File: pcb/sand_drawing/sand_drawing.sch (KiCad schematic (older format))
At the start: 19 parts, among them J0 12V GND, J1 Stepper1, J2 Stepper2, J3 Opto 1, J4 Opto 2, J5 ESP POWER, J6 Unused Pins, U1 WeMos_D1_mini, U2 LD1117

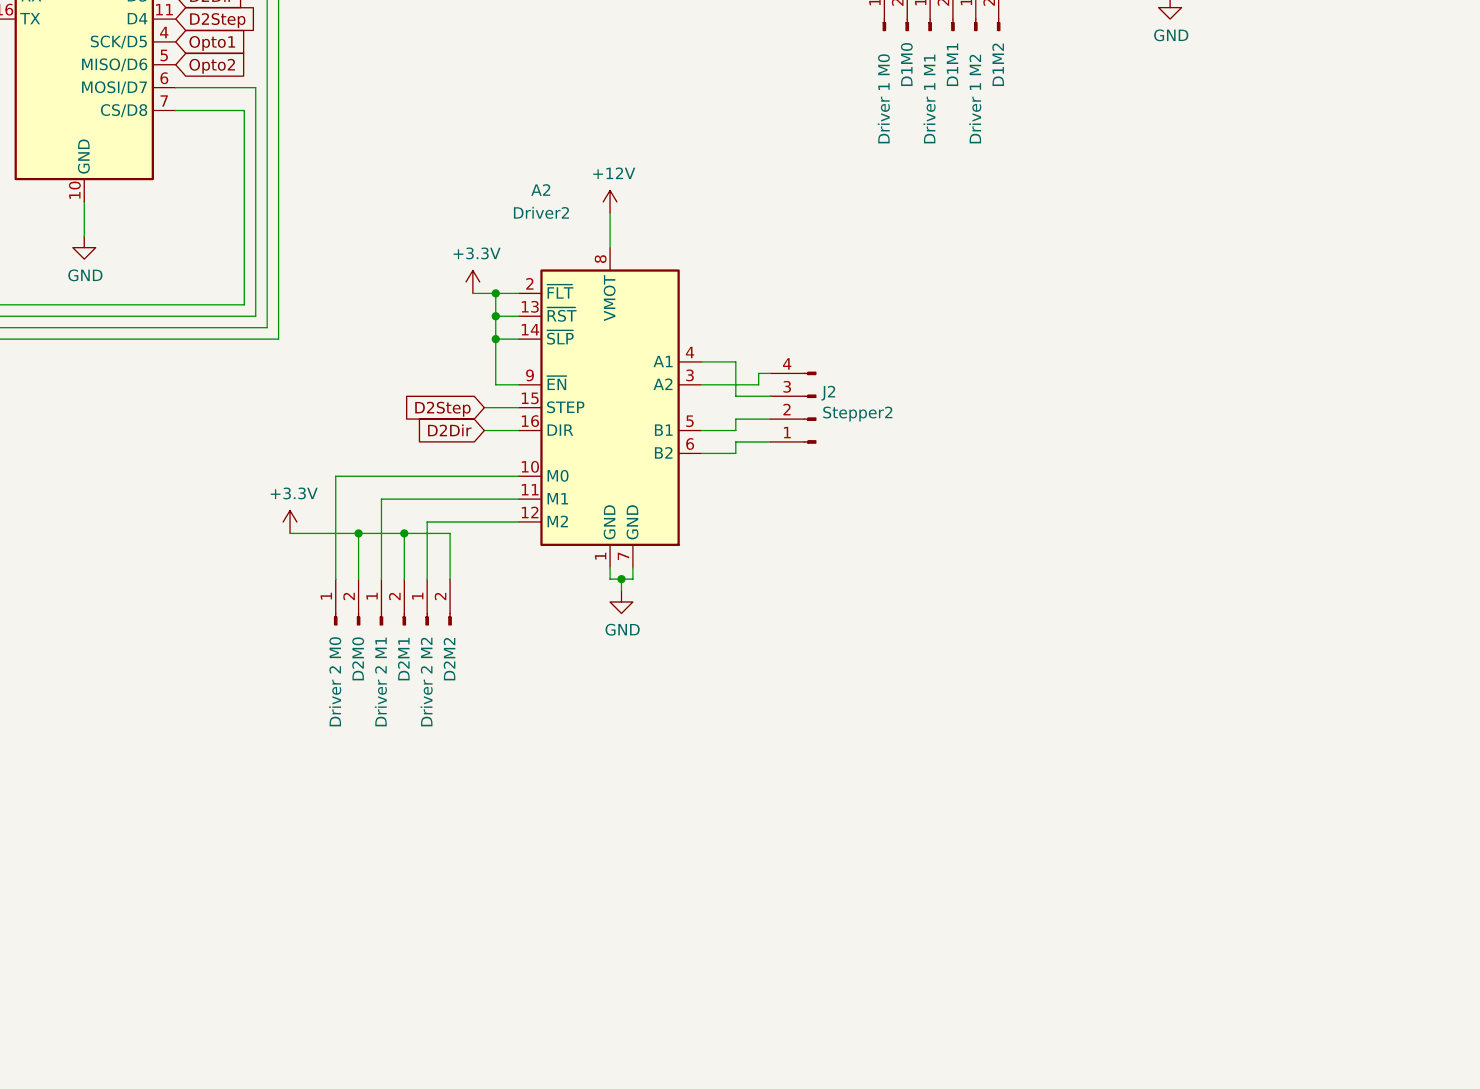
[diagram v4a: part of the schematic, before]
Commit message: More work on adding the esp32 .
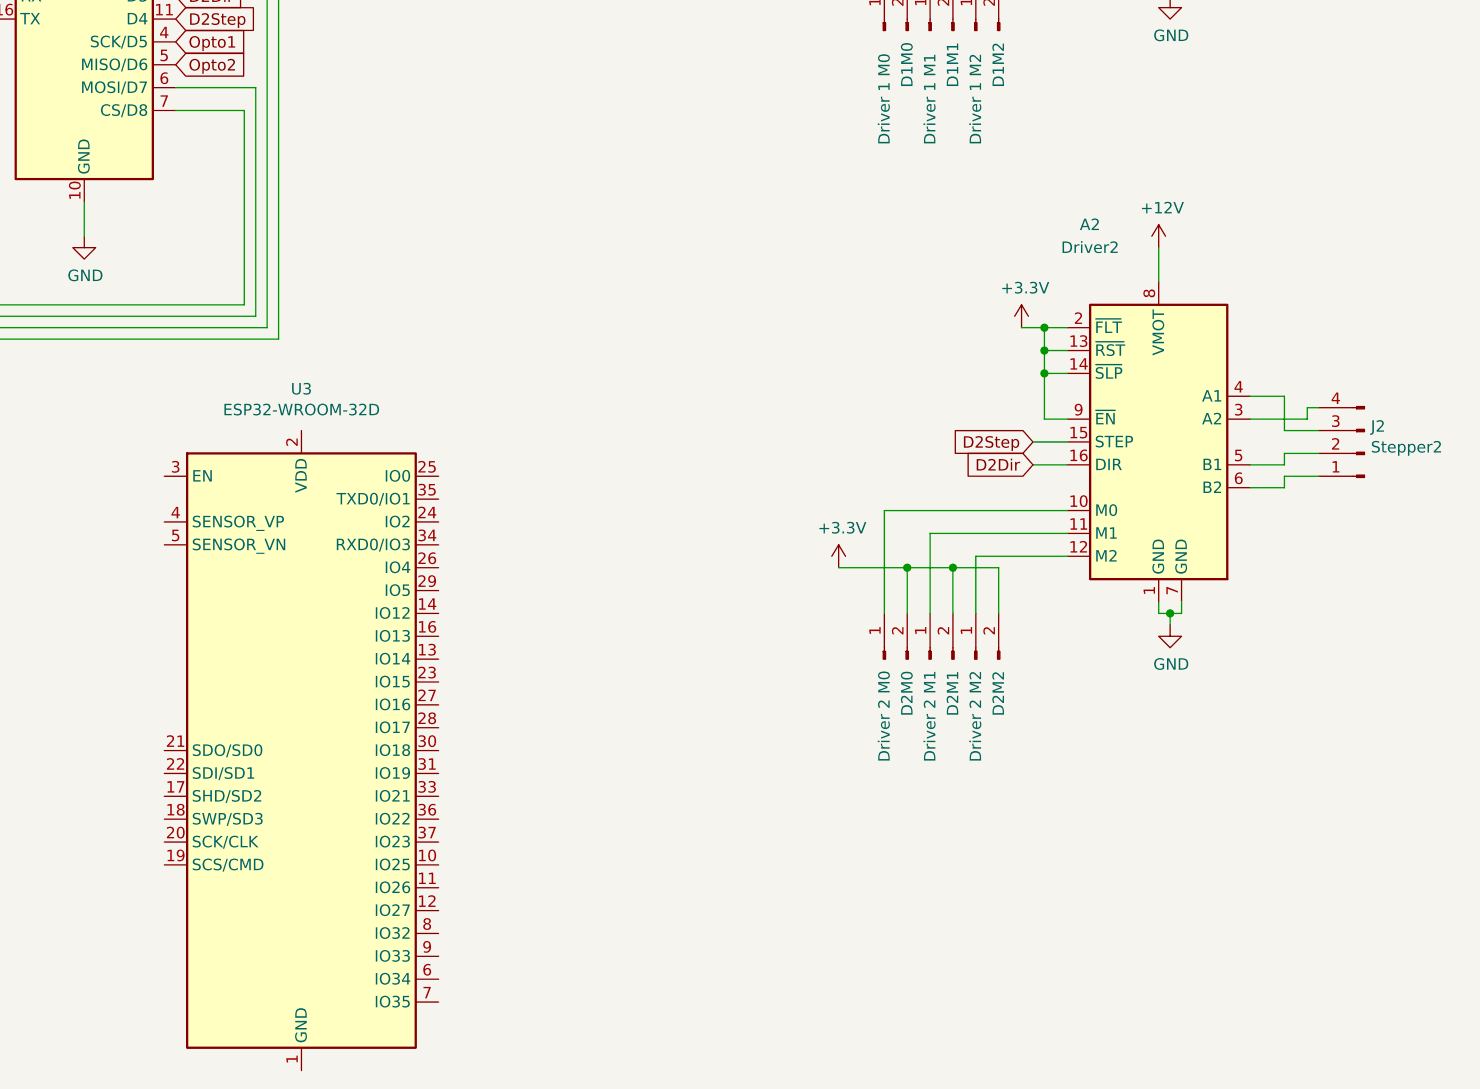
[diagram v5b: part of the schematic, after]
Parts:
- added U3: ESP32-WROOM-32D, Custom:ESP32-WROOM-32, symbol RF_Module:ESP32-WROOM-32D
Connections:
- new net: U3.1 (GND), U3.15 (GND), U3.38 (GND), U3.39 (GND)
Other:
- moved on the sheet: A2, D2M0, D2M1, D2M2, J2
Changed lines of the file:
@@
 L Driver_Motor:Pololu_Breakout_DRV8825 A2
 U 1 1 5E987B88
-P 5600 4200
-F 0 "A2" H 5300 5050 50  0000 C CNN
-F 1 "Driver2" H 5300 4950 50  0000 C CNN
-F 2 "Modules:Pololu_Breakout-16_15.2x20.3mm" H 5800 3400 50  0001 L CNN
-F 3 "https://www.pololu.com/product/2982" H 5700 3900 50  0001 C CNN
-	1    5600 4200
+P 8000 4350
+F 0 "A2" H 7700 5200 50  0000 C CNN
+F 1 "Driver2" H 7700 5100 50  0000 C CNN
+F 2 "Modules:Pololu_Breakout-16_15.2x20.3mm" H 8200 3550 50  0001 L CNN
+F 3 "https://www.pololu.com/product/2982" H 8100 4050 50  0001 C CNN
+	1    8000 4350
 	1    0    0    -1
 $EndComp
@@
 L Connector:Conn_01x04_Male J2
 U 1 1 5E98E54C
-P 6500 4350
-F 0 "J2" H 6472 4232 50  0000 R CNN
-F 1 "Stepper2" H 6472 4323 50  0000 R CNN
-F 2 "Socket_Strips:Socket_Strip_Straight_1x04_Pitch2.54mm" H 6500 4350 50  0001 C CNN
-F 3 "~" H 6500 4350 50  0001 C CNN
-	1    6500 4350
+P 8900 4500
+F 0 "J2" H 8872 4382 50  0000 R CNN
+F 1 "Stepper2" H 8872 4473 50  0000 R CNN
+F 2 "Socket_Strips:Socket_Strip_Straight_1x04_Pitch2.54mm" H 8900 4500 50  0001 C CNN
+F 3 "~" H 8900 4500 50  0001 C CNN
+	1    8900 4500
 	-1   0    0    1
 $EndComp
@@
 	8550 1850 8700 1850
 Wire Wire Line
-	6000 4100 6150 4100
-Wire Wire Line
-	6000 4400 6150 4400
-Wire Wire Line
-	6150 4400 6150 4350
-Wire Wire Line
-	6150 4350 6300 4350
-Wire Wire Line
-	6000 4500 6150 4500
-Wire Wire Line
-	6150 4500 6150 4450
-Wire Wire Line
-	6150 4450 6300 4450
+	8400 4250 8550 4250
+Wire Wire Line
+	8400 4550 8550 4550
+Wire Wire Line
+	8550 4550 8550 4500
+Wire Wire Line
+	8550 4500 8700 4500
+Wire Wire Line
+	8400 4650 8550 4650
+Wire Wire Line
+	8550 4650 8550 4600
+Wire Wire Line
+	8550 4600 8700 4600
 Wire Wire Line
 	7500 1200 7400 1200
 Wire Wire Line
-	5200 4200 5100 4200
-Wire Wire Line
-	5200 4000 5100 4000
-Wire Wire Line
-	5100 4000 5100 4200
-Wire Wire Line
-	5200 3900 5100 3900
-Wire Wire Line
-	5100 3900 5100 4000
-Connection ~ 5100 4000
-Wire Wire Line
-	5100 3800 5100 3900
-Connection ~ 5100 3900
+	7600 4350 7500 4350
+Wire Wire Line
+	7600 4150 7500 4150
+Wire Wire Line
+	7500 4150 7500 4350
+Wire Wire Line
+	7600 4050 7500 4050
+Wire Wire Line
+	7500 4050 7500 4150
+Connection ~ 7500 4150
+Wire Wire Line
+	7500 3950 7500 4050
+Connection ~ 7500 4050
 Wire Wire Line
 	7600 1600 7500 1600
@@
 L power:GND #PWR0101
 U 1 1 5E9A89B2
-P 5650 5100
-F 0 "#PWR0101" H 5650 4850 50  0001 C CNN
-F 1 "GND" H 5655 4927 50  0000 C CNN
-F 2 "" H 5650 5100 50  0001 C CNN
-F 3 "" H 5650 5100 50  0001 C CNN
-	1    5650 5100
+P 8050 5250
+F 0 "#PWR0101" H 8050 5000 50  0001 C CNN
+F 1 "GND" H 8055 5077 50  0000 C CNN
+F 2 "" H 8050 5250 50  0001 C CNN
+F 3 "" H 8050 5250 50  0001 C CNN
+	1    8050 5250
 	1    0    0    -1
 $EndComp
@@
 Connection ~ 8050 2450
 Wire Wire Line
-	5600 5000 5600 5050
-Wire Wire Line
-	5600 5050 5650 5050
-Wire Wire Line
-	5650 5050 5650 5100
-Wire Wire Line
-	5650 5050 5700 5050
-Wire Wire Line
-	5700 5050 5700 5000
-Connection ~ 5650 5050
+	8000 5150 8000 5200
+Wire Wire Line
+	8000 5200 8050 5200
+Wire Wire Line
+	8050 5200 8050 5250
+Wire Wire Line
+	8050 5200 8100 5200
+Wire Wire Line
+	8100 5200 8100 5150
+Connection ~ 8050 5200
 $Comp
 L power:+12V #PWR0103
 U 1 1 5E9C6646
-P 5600 3450
-F 0 "#PWR0103" H 5600 3300 50  0001 C CNN
-F 1 "+12V" H 5615 3623 50  0000 C CNN
-F 2 "" H 5600 3450 50  0001 C CNN
-F 3 "" H 5600 3450 50  0001 C CNN
-	1    5600 3450
+P 8000 3600
+F 0 "#PWR0103" H 8000 3450 50  0001 C CNN
+F 1 "+12V" H 8015 3773 50  0000 C CNN
+F 2 "" H 8000 3600 50  0001 C CNN
+F 3 "" H 8000 3600 50  0001 C CNN
+	1    8000 3600
 	1    0    0    -1
 $EndComp
@@
 Connection ~ 7500 1200
 Wire Wire Line
-	5200 3800 5100 3800
-Wire Wire Line
-	5000 3800 5100 3800
-Connection ~ 5100 3800
+	7600 3950 7500 3950
+Wire Wire Line
+	7400 3950 7500 3950
+Connection ~ 7500 3950
 $Comp
 L Connector:Conn_01x03_Male J3
@@
 L power:+3.3V #PWR0108
 U 1 1 5E9FDAD5
-P 5000 3800
-F 0 "#PWR0108" H 5000 3650 50  0001 C CNN
-F 1 "+3.3V" H 5015 3973 50  0000 C CNN
-F 2 "" H 5000 3800 50  0001 C CNN
-F 3 "" H 5000 3800 50  0001 C CNN
-	1    5000 3800
+P 7400 3950
+F 0 "#PWR0108" H 7400 3800 50  0001 C CNN
+F 1 "+3.3V" H 7415 4123 50  0000 C CNN
+F 2 "" H 7400 3950 50  0001 C CNN
+F 3 "" H 7400 3950 50  0001 C CNN
+	1    7400 3950
 	1    0    0    -1
 $EndComp
@@
 	8600 1550 8700 1550
 Wire Wire Line
-	6150 4250 6300 4250
-Wire Wire Line
-	6150 4100 6150 4250
-Wire Wire Line
-	6300 4150 6250 4150
-Wire Wire Line
-	6250 4150 6250 4200
-Wire Wire Line
-	6250 4200 6000 4200
+	8550 4400 8700 4400
+Wire Wire Line
+	8550 4250 8550 4400
+Wire Wire Line
+	8700 4300 8650 4300
+Wire Wire Line
+	8650 4300 8650 4350
+Wire Wire Line
+	8650 4350 8400 4350
 $Comp
 L Connector_Generic:Conn_02x04_Top_Bottom J6
@@
 L Connector:Conn_01x02_Male D2M1
 U 1 1 5E9C5CF2
-P 4600 5250
-F 0 "D2M1" H 4450 5150 50  0000 C CNN
-F 1 "Driver 2 M1" H 4350 5250 50  0000 C CNN
-F 2 "Socket_Strips:Socket_Strip_Straight_1x02_Pitch2.54mm" H 4600 5250 50  0001 C CNN
-F 3 "~" H 4600 5250 50  0001 C CNN
-	1    4600 5250
+P 7000 5400
+F 0 "D2M1" H 6850 5300 50  0000 C CNN
+F 1 "Driver 2 M1" H 6750 5400 50  0000 C CNN
+F 2 "Socket_Strips:Socket_Strip_Straight_1x02_Pitch2.54mm" H 7000 5400 50  0001 C CNN
+F 3 "~" H 7000 5400 50  0001 C CNN
+	1    7000 5400
 	0    -1   -1   0
 $EndComp
@@
 L Connector:Conn_01x02_Male D2M2
 U 1 1 5E9C5F13
-P 4800 5250
-F 0 "D2M2" H 4650 5150 50  0000 C CNN
-F 1 "Driver 2 M2" H 4550 5250 50  0000 C CNN
-F 2 "Socket_Strips:Socket_Strip_Straight_1x02_Pitch2.54mm" H 4800 5250 50  0001 C CNN
-F 3 "~" H 4800 5250 50  0001 C CNN
-	1    4800 5250
+P 7200 5400
+F 0 "D2M2" H 7050 5300 50  0000 C CNN
+F 1 "Driver 2 M2" H 6950 5400 50  0000 C CNN
+F 2 "Socket_Strips:Socket_Strip_Straight_1x02_Pitch2.54mm" H 7200 5400 50  0001 C CNN
+F 3 "~" H 7200 5400 50  0001 C CNN
+	1    7200 5400
 	0    -1   -1   0
 $EndComp
@@
 	1400 5550 1400 4800
 Wire Wire Line
-	5200 4600 4400 4600
-Wire Wire Line
-	4400 4600 4400 5050
-Wire Wire Line
-	4600 5050 4600 4700
-Wire Wire Line
-	4600 4700 5200 4700
-Wire Wire Line
-	5200 4800 4800 4800
-Wire Wire Line
-	4800 4800 4800 5050
+	7600 4750 6800 4750
+Wire Wire Line
+	6800 4750 6800 5200
+Wire Wire Line
+	7000 5200 7000 4850
+Wire Wire Line
+	7000 4850 7600 4850
+Wire Wire Line
+	7600 4950 7200 4950
+Wire Wire Line
+	7200 4950 7200 5200
 $Comp
 L power:+3.3V #PWR0116
 U 1 1 5EA0D498
-P 4200 4850
-F 0 "#PWR0116" H 4200 4700 50  0001 C CNN
-F 1 "+3.3V" H 4215 5023 50  0000 C CNN
-F 2 "" H 4200 4850 50  0001 C CNN
-F 3 "" H 4200 4850 50  0001 C CNN
-	1    4200 4850
-	1    0    0    -1
-$EndComp
-Wire Wire Line
-	4500 4850 4500 5050
-Wire Wire Line
-	4900 4850 4900 5050
-Wire Wire Line
-	4500 4850 4700 4850
-Connection ~ 4500 4850
-Wire Wire Line
-	4700 5050 4700 4850
-Connection ~ 4700 4850
-Wire Wire Line
-	4700 4850 4900 4850
-Wire Wire Line
-	4200 4850 4500 4850
+P 6600 5000
+F 0 "#PWR0116" H 6600 4850 50  0001 C CNN
+F 1 "+3.3V" H 6615 5173 50  0000 C CNN
+F 2 "" H 6600 5000 50  0001 C CNN
+F 3 "" H 6600 5000 50  0001 C CNN
+	1    6600 5000
+	1    0    0    -1
+$EndComp
+Wire Wire Line
+	6900 5000 6900 5200
+Wire Wire Line
+	7300 5000 7300 5200
+Wire Wire Line
+	6900 5000 7100 5000
+Connection ~ 6900 5000
+Wire Wire Line
+	7100 5200 7100 5000
+Connection ~ 7100 5000
+Wire Wire Line
+	7100 5000 7300 5000
+Wire Wire Line
+	6600 5000 6900 5000
 Wire Wire Line
 	8000 850  8000 1000
 Wire Wire Line
-	5600 3600 5600 3450
+	8000 3750 8000 3600
 $Comp
 L Connector:Conn_01x02_Male D1M0
@@
 L Connector:Conn_01x02_Male D2M0
 U 1 1 5E99CB34
-P 4400 5250
-F 0 "D2M0" H 4250 5150 50  0000 C CNN
-F 1 "Driver 2 M0" H 4150 5250 50  0000 C CNN
-F 2 "Socket_Strips:Socket_Strip_Straight_1x02_Pitch2.54mm" H 4400 5250 50  0001 C CNN
-F 3 "~" H 4400 5250 50  0001 C CNN
-	1    4400 5250
+P 6800 5400
+F 0 "D2M0" H 6650 5300 50  0000 C CNN
+F 1 "Driver 2 M0" H 6550 5400 50  0000 C CNN
+F 2 "Socket_Strips:Socket_Strip_Straight_1x02_Pitch2.54mm" H 6800 5400 50  0001 C CNN
+F 3 "~" H 6800 5400 50  0001 C CNN
+	1    6800 5400
 	0    -1   -1   0
 $EndComp
@@
 Text GLabel 3700 2600 2    50   Input ~ 0
 D2Step
-Text GLabel 5050 4400 0    50   Input ~ 0
+Text GLabel 7450 4550 0    50   Input ~ 0
 D2Dir
-Text GLabel 5050 4300 0    50   Input ~ 0
+Text GLabel 7450 4450 0    50   Input ~ 0
 D2Step
 Wire Wire Line
-	5200 4300 5050 4300
-Wire Wire Line
-	5200 4400 5050 4400
+	7600 4450 7450 4450
+Wire Wire Line
+	7600 4550 7450 4550
 $Comp
 L Connector:Conn_01x02_Male D1M2
@@
 	0    -1   -1   0
 $EndComp
+$Comp
+L RF_Module:ESP32-WROOM-32D U3
+U 1 1 5EC68010
+P 4250 5800
+F 0 "U3" H 4250 7381 50  0000 C CNN
+F 1 "ESP32-WROOM-32D" H 4250 7290 50  0000 C CNN
+F 2 "Custom:ESP32-WROOM-32" H 4250 4300 50  0001 C CNN
+F 3 "https://www.espressif.com/sites/default/files/documentation/esp32-wroom-32d_esp32-wroom-32u_datasheet_en.pdf" H 3950 5850 50  0001 C CNN
+	1    4250 5800
+	1    0    0    -1
+$EndComp
 $EndSCHEMATC

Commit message: Assigning JLCPCB parts store codes to stuff.
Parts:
- removed D1M0: Driver 1 M0, Socket_Strips:Socket_Strip_Straight_1x02_Pitch2.54mm, symbol Connector:Conn_01x02_Male
- removed D1M1: Driver 1 M1, Socket_Strips:Socket_Strip_Straight_1x02_Pitch2.54mm, symbol Connector:Conn_01x02_Male
- removed D1M2: Driver 1 M2, Socket_Strips:Socket_Strip_Straight_1x02_Pitch2.54mm, symbol Connector:Conn_01x02_Male
- removed D2M0: Driver 2 M0, Socket_Strips:Socket_Strip_Straight_1x02_Pitch2.54mm, symbol Connector:Conn_01x02_Male
- removed D2M1: Driver 2 M1, Socket_Strips:Socket_Strip_Straight_1x02_Pitch2.54mm, symbol Connector:Conn_01x02_Male
- removed D2M2: Driver 2 M2, Socket_Strips:Socket_Strip_Straight_1x02_Pitch2.54mm, symbol Connector:Conn_01x02_Male
- removed J5: ESP POWER, Socket_Strips:Socket_Strip_Straight_1x02_Pitch2.54mm, symbol Connector:Conn_01x02_Male
- removed J6: Unused Pins, Socket_Strips:Socket_Strip_Straight_2x04_Pitch2.54mm, symbol Connector_Generic:Conn_02x04_Top_Bottom
- removed U1: WeMos_D1_mini, Custom:WEMOS_D1_mini_light, symbol MCU_Module:WeMos_D1_mini
- added D1, D10, D11, D12, D13, D14, D15, D16, D17, D18, D2, D3, D4, D5, D6, D7, D8, D9: SS210 Schottky Diode, Diode_SMD:D_SMA, symbol Device:D_Schottky_Small
- added J5: UART, Socket_Strips:Socket_Strip_Straight_1x03_Pitch2.54mm, symbol Connector:Conn_01x03_Male
- added J6: ESP POWER, Socket_Strips:Socket_Strip_Straight_1x02_Pitch2.54mm, symbol Connector:Conn_01x02_Male
- A1, A2: symbol Driver_Motor:Pololu_Breakout_DRV8825 -> pololu_breakout_tmc2100:Pololu_Breakout_tmc2100
- C1: value 0.1µF -> 10µF/25V; footprint Capacitors_THT:C_Axial_L3.8mm_D2.6mm_P7.50mm_Horizontal -> Capacitor_SMD:C_0805_2012Metric; LCSC (none) -> C15850
- C2: value 10µF -> 10µF/25V; footprint Capacitors_THT:C_Axial_L3.8mm_D2.6mm_P7.50mm_Horizontal -> Capacitor_SMD:C_0805_2012Metric; LCSC (none) -> C15850
- U2: value LD1117 -> AMS1117-3.3; footprint Power_Integrations:TO-220 -> Package_TO_SOT_SMD:SOT-223; LCSC (none) -> C6186
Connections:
- net +12V: now also D13.1 (K), D14.1 (K), D15.1 (K), D16.1 (K), D17.1 (K), D18.1 (K), D5.1 (K), D6.1 (K), D7.1 (K), D8.1 (K)
- net +3V3: now also D17.2 (A), D18.2 (A), J6.2 (Pin_2); no longer A1.13 (~RST), A1.14 (~SLP), A1.9 (~EN), A2.13 (~RST), A2.14 (~SLP), A2.9 (~EN)
- net D1Dir: now also U3.26 (IO4)
- net D1Step: now also U3.27 (IO16)
- net D2Dir: now also U3.7 (IO35)
- net D2Step: now also U3.8 (IO32)
- net GND: now also U3.1 (GND), U3.15 (GND), U3.38 (GND), U3.39 (GND), D1.2 (A), D10.2 (A), D11.2 (A), D12.2 (A), D2.2 (A), D3.2 (A), D4.2 (A), D9.2 (A), J5.1 (Pin_1); no longer J3.1 (Pin_1), J4.1 (Pin_1)
- net Opto1: now also U3.4 (SENSOR_VP)
- net Opto2: now also U3.5 (SENSOR_VN)
- net D1CFG1: now reaches A1.10 (CFG1)
- net D1CFG1: now also U3.30 (IO18)
- net D1CFG2: now reaches A1.11 (CFG2)
- net D1CFG2: now also U3.29 (IO5)
- net D1CFG3: now reaches A1.12 (CFG3)
- net D1CFG3: now also U3.28 (IO17)
- net at A1.3 (A2), J1.4 (Pin_4): now also D12.1 (K), D16.2 (A)
- net at A1.4 (A1), J1.3 (Pin_3): now also D11.1 (K), D15.2 (A)
- net at A1.5 (B1), J1.2 (Pin_2): now also D10.1 (K), D14.2 (A)
- net at A1.6 (B2), J1.1 (Pin_1): now also D13.2 (A), D9.1 (K)
- net D2CFG1: now reaches A2.10 (CFG1)
- net D2CFG1: now also U3.11 (IO26)
- net D2CFG2: now reaches A2.11 (CFG2)
- net D2CFG2: now also U3.10 (IO25)
- net D2CFG3: now reaches A2.12 (CFG3)
- net D2CFG3: now also U3.9 (IO33)
- net at A2.3 (A2), J2.4 (Pin_4): now also D4.1 (K), D8.2 (A)
- net at A2.4 (A1), J2.3 (Pin_3): now also D3.1 (K), D7.2 (A)
- net at A2.5 (B1), J2.2 (Pin_2): now also D2.1 (K), D6.2 (A)
- net at A2.6 (B2), J2.1 (Pin_1): now also D1.1 (K), D5.2 (A)
- net D2Enable: now reaches U3.12 (IO27)
- net D2Enable: now also A2.9 (~EN)
- net at U3.2 (VDD): now also J6.1 (Pin_1)
- net Reserved: now reaches U3.25 (IO0)
- net Reserved: now also U3.3 (EN)
- net D1Enable: now reaches U3.31 (IO19)
- net D1Enable: now also A1.9 (~EN)
- net RX: now reaches U3.34 (RXD0/IO3)
- net RX: now also J5.2 (Pin_2)
- net TX: now reaches U3.35 (TXD0/IO1)
- net TX: now also J5.3 (Pin_3)
- new net: J3.1 (Pin_1), J4.1 (Pin_1)
- no-connect marks 0 -> 6
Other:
- note added: "I know the pin assignments for the stepper drivers looks weird.\nIt's this way to ensure the control signals can be bussed together\nfor a neat layout.\nAlso see https://randomnerdtutorials.com/esp32-pinout-reference-gpios/"
- note added: "Protection circuit from https://learn.watterott.com/silentstepstick/protector/"
- note added: "Stepper pinout order:\nEN\nCFG1\nCFG2\nCFG3\nNC\nNC\nSTEP\nDIR"
- moved on the sheet: J1, J2, J3, J4, U3
